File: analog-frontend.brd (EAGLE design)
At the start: 28.4 x 25.2 mm, 69 parts, among them IC1 TPS63031, IC2 ADG731, IC3 TM4C123G, IC4 INA332, IC5 NRF24L01SMD, IC6 OPA2320, Y1 CRYSTAL3X2, Y2 CRYSTAL3X2

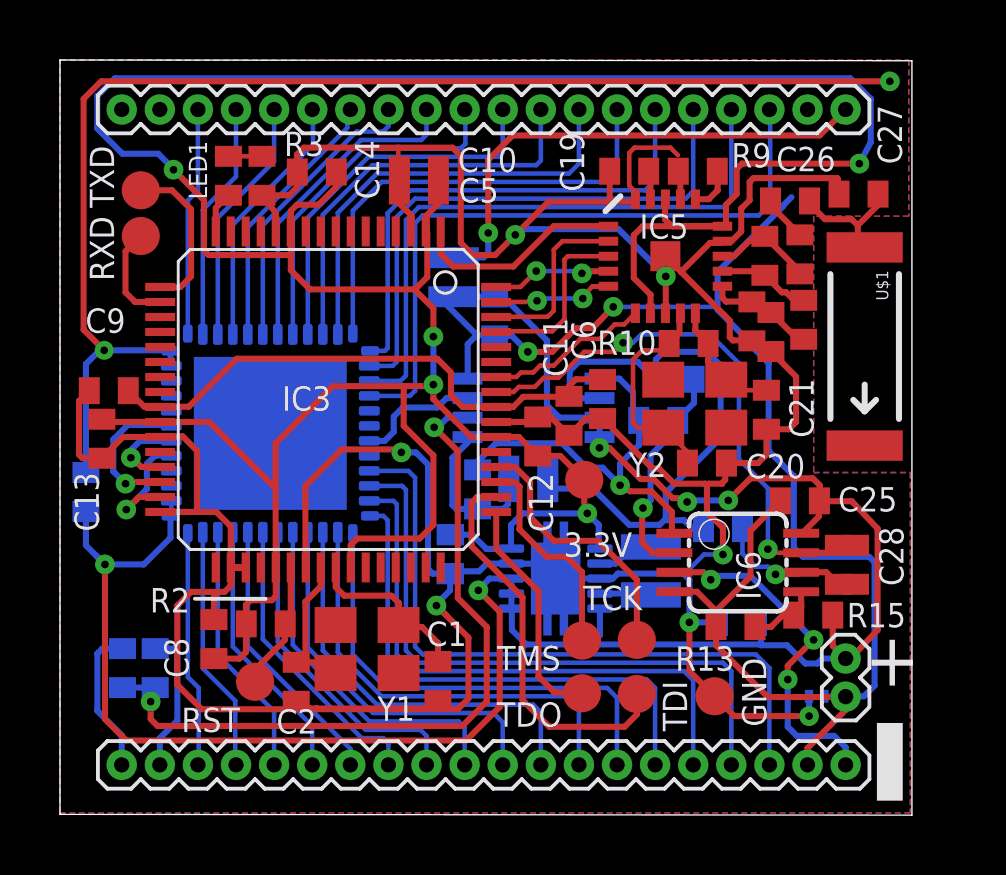
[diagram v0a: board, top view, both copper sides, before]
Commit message: added component values
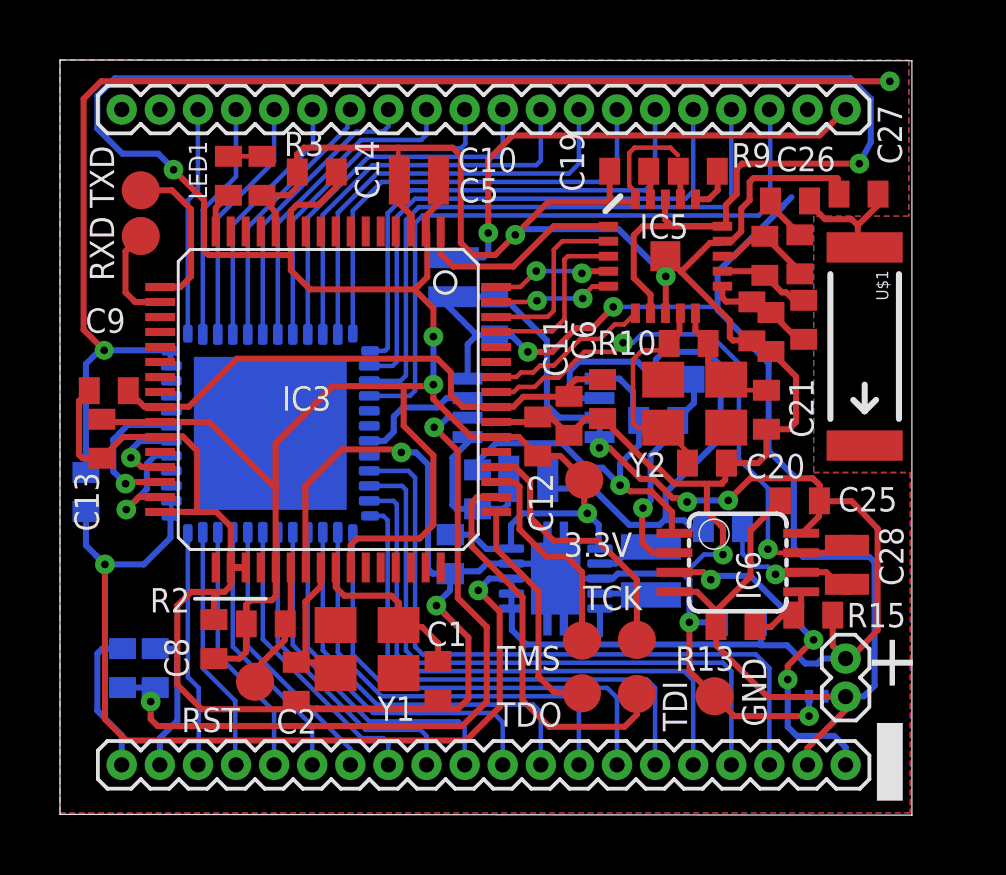
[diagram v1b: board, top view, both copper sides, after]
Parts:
- C10: value (none) -> 0.01u
- C11: value (none) -> 2.2u
- C12, C13, C15, C17, C5, C8, C9: value (none) -> 0.1u
- C14, C6: value (none) -> 1.0u
- C3: value (none) -> 4.7u
- C4, C7: value (none) -> 10u
- R2: value (none) -> 10k
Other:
- board outline removed
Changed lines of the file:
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@@
 <?xml version="1.0" encoding="utf-8"?>
 <!DOCTYPE eagle SYSTEM "eagle.dtd">
-<eagle version="6.5.0">
+<eagle version="6.6.0">
 <drawing>
 <settings>
@@
 <board>
 <plain>
-<wire x1="0" y1="0" x2="28.3972" y2="-0.0254" width="0" layer="20"/>
-<wire x1="28.3972" y1="-0.0254" x2="28.3972" y2="25.1206" width="0" layer="20"/>
-<wire x1="28.3972" y1="25.1206" x2="0" y2="25.146" width="0" layer="20"/>
-<wire x1="0" y1="25.146" x2="0" y2="0" width="0" layer="20"/>
+<wire x1="0" y1="0" x2="28.3972" y2="-0.0254" width="0" layer="21"/>
+<wire x1="28.3972" y1="-0.0254" x2="28.3972" y2="25.1206" width="0" layer="21"/>
+<wire x1="28.3972" y1="25.1206" x2="0" y2="25.146" width="0" layer="21"/>
+<wire x1="0" y1="25.146" x2="0" y2="0" width="0" layer="21"/>
 <wire x1="4.4958" y1="7.1882" x2="6.858" y2="7.1882" width="0.127" layer="25"/>
 <text x="26.8224" y="4.2926" size="1.778" layer="25">+</text>
 <text x="28.067" y="4.2926" size="1.778" layer="26" rot="MR0">+</text>
 <rectangle x1="27.2288" y1="0.4572" x2="28.0924" y2="3.048" layer="25"/>
+<wire x1="0" y1="0" x2="28.3972" y2="0" width="0" layer="22"/>
+<wire x1="28.3972" y1="0" x2="28.3972" y2="25.1206" width="0" layer="22"/>
+<wire x1="28.3972" y1="25.1206" x2="0" y2="25.1206" width="0" layer="22"/>
+<wire x1="0" y1="25.1206" x2="0" y2="0" width="0" layer="22"/>
 </plain>
 <attributes>
@@
 <attribute name="NAME" x="20.2057" y="5.8801" size="0.8128" layer="26" rot="MR0"/>
 </element>
-<element name="C3" library="rcl" package="C0402" value="" x="22.5679" y="6.4008" smashed="yes" rot="MR0">
+<element name="C3" library="rcl" package="C0402" value="4.7u" x="22.5679" y="6.4008" smashed="yes" rot="MR0">
 <attribute name="NAME" x="25.1587" y="6.6294" size="0.8128" layer="26" rot="MR0"/>
 <attribute name="VALUE" x="23.2029" y="4.4958" size="1.27" layer="28" rot="MR0"/>
 </element>
-<element name="C4" library="rcl" package="C0402" value="" x="13.0048" y="8.6741" smashed="yes" rot="MR270">
+<element name="C4" library="rcl" package="C0402" value="10u" x="13.0048" y="8.6741" smashed="yes" rot="MR270">
 <attribute name="NAME" x="12.3571" y="7.7978" size="0.8128" layer="26" rot="MR0"/>
 <attribute name="VALUE" x="14.9098" y="9.3091" size="1.27" layer="28" rot="MR270"/>
 </element>
-<element name="C7" library="rcl" package="C0402" value="" x="13.0175" y="8.6741" smashed="yes" rot="MR270">
+<element name="C7" library="rcl" package="C0402" value="10u" x="13.0175" y="8.6741" smashed="yes" rot="MR270">
 <attribute name="NAME" x="12.3063" y="8.8265" size="0.8128" layer="26" rot="MR0"/>
 <attribute name="VALUE" x="14.9225" y="9.3091" size="1.27" layer="28" rot="MR270"/>
@@
 <attribute name="VALUE" x="19.304" y="15.0368" size="1.27" layer="28" rot="MR180"/>
 </element>
-<element name="C17" library="rcl" package="C0402" value="" x="14.4907" y="16.5989" smashed="yes" rot="MR90">
+<element name="C17" library="rcl" package="C0402" value="0.1u" x="14.4907" y="16.5989" smashed="yes" rot="MR90">
 <attribute name="NAME" x="14.8209" y="16.6751" size="0.8128" layer="26" rot="MR180"/>
 <attribute name="VALUE" x="12.5857" y="15.9639" size="1.27" layer="28" rot="MR90"/>
@@
 <attribute name="VALUE" x="25.7429" y="8.5471" size="1.27" layer="27" rot="R180"/>
 </element>
-<element name="C15" library="rcl" package="C0402" value="" x="0.8636" y="10.7442" smashed="yes" rot="MR90">
+<element name="C15" library="rcl" package="C0402" value="0.1u" x="0.8636" y="10.7442" smashed="yes" rot="MR90">
 <attribute name="NAME" x="0.9144" y="11.9888" size="0.8128" layer="26" rot="MR90"/>
 <attribute name="VALUE" x="-1.0414" y="10.1092" size="1.27" layer="28" rot="MR90"/>
@@
 <attribute name="VALUE" x="5.969" y="5.0546" size="1.27" layer="27" rot="R270"/>
 </element>
-<element name="C6" library="rcl" package="C0402" value="" x="18.0848" y="13.843" smashed="yes" rot="R270">
+<element name="C6" library="rcl" package="C0402" value="1.0u" x="18.0848" y="13.843" smashed="yes" rot="R270">
 <attribute name="NAME" x="17.8562" y="15.1384" size="0.8128" layer="25" rot="R90"/>
 <attribute name="VALUE" x="16.1798" y="14.478" size="1.27" layer="27" rot="R270"/>
 </element>
-<element name="C9" library="rcl" package="C0402" value="" x="1.6256" y="14.1224" smashed="yes" rot="R180">
+<element name="C9" library="rcl" package="C0402" value="0.1u" x="1.6256" y="14.1224" smashed="yes" rot="R180">
 <attribute name="NAME" x="2.1844" y="16.8656" size="0.8128" layer="25" rot="R180"/>
 <attribute name="VALUE" x="2.2606" y="16.0274" size="1.27" layer="27" rot="R180"/>
 </element>
-<element name="C11" library="rcl" package="C0402" value="" x="16.9672" y="13.2842" smashed="yes" rot="R270">
+<element name="C11" library="rcl" package="C0402" value="2.2u" x="16.9672" y="13.2842" smashed="yes" rot="R270">
 <attribute name="NAME" x="16.9164" y="14.5796" size="0.8128" layer="25" rot="R90"/>
 <attribute name="VALUE" x="15.0622" y="13.9192" size="1.27" layer="27" rot="R270"/>
 </element>
-<element name="C5" library="rcl" package="C0402" value="" x="11.9634" y="20.7772" smashed="yes" rot="R180">
+<element name="C5" library="rcl" package="C0402" value="0.1u" x="11.9634" y="20.7772" smashed="yes" rot="R180">
 <attribute name="NAME" x="13.2842" y="20.3962" size="0.8128" layer="25"/>
 <attribute name="VALUE" x="12.5984" y="22.6822" size="1.27" layer="27" rot="R180"/>
 </element>
-<element name="C8" library="rcl" package="C0402" value="" x="5.1308" y="5.842" smashed="yes" rot="R90">
+<element name="C8" library="rcl" package="C0402" value="0.1u" x="5.1308" y="5.842" smashed="yes" rot="R90">
 <attribute name="NAME" x="4.2926" y="4.5466" size="0.8128" layer="25" rot="R90"/>
 <attribute name="VALUE" x="7.0358" y="5.207" size="1.27" layer="27" rot="R90"/>
 </element>
-<element name="C10" library="rcl" package="C0402" value="" x="11.9634" y="21.4884" smashed="yes" rot="R180">
+<element name="C10" library="rcl" package="C0402" value="0.01u" x="11.9634" y="21.4884" smashed="yes" rot="R180">
 <attribute name="NAME" x="13.2588" y="21.4122" size="0.8128" layer="25"/>
 <attribute name="VALUE" x="12.5984" y="23.3934" size="1.27" layer="27" rot="R180"/>
 </element>
-<element name="C12" library="rcl" package="C0402" value="" x="15.9258" y="12.5984" smashed="yes" rot="R90">
+<element name="C12" library="rcl" package="C0402" value="0.1u" x="15.9258" y="12.5984" smashed="yes" rot="R90">
 <attribute name="NAME" x="15.621" y="11.3792" size="0.8128" layer="25" rot="R270"/>
 <attribute name="VALUE" x="17.8308" y="11.9634" size="1.27" layer="27" rot="R90"/>
 </element>
-<element name="C13" library="rcl" package="C0402" value="" x="1.397" y="12.5222" smashed="yes" rot="R270">
+<element name="C13" library="rcl" package="C0402" value="0.1u" x="1.397" y="12.5222" smashed="yes" rot="R270">
 <attribute name="NAME" x="0.4826" y="11.4046" size="0.8128" layer="25" rot="R270"/>
 <attribute name="VALUE" x="-0.508" y="13.1572" size="1.27" layer="27" rot="R270"/>
 </element>
-<element name="C14" library="rcl" package="C0402" value="" x="8.5598" y="21.4122" smashed="yes" rot="R180">
+<element name="C14" library="rcl" package="C0402" value="1.0u" x="8.5598" y="21.4122" smashed="yes" rot="R180">
 <attribute name="NAME" x="9.8298" y="22.479" size="0.8128" layer="25" rot="R270"/>
 <attribute name="VALUE" x="9.1948" y="23.3172" size="1.27" layer="27" rot="R180"/>
 </element>
-<element name="R2" library="rcl" package="R0402" value="" x="6.858" y="6.35" smashed="yes">
+<element name="R2" library="rcl" package="R0402" value="10k" x="6.858" y="6.35" smashed="yes">
 <attribute name="NAME" x="2.9972" y="6.731" size="0.8128" layer="25"/>
 <attribute name="VALUE" x="6.223" y="4.445" size="1.27" layer="27"/>

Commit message: fixed component values
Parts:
- C1, C2, C20, C21, C28: value (none) -> 22p
- C18: value (none) -> 10p
- C19: value (none) -> 33n
- C22: value (none) -> 2.2n
- C23: value (none) -> 10n
- C24: value (none) -> 4.7p
- C25: value (none) -> 0.1u
- C26: value (none) -> 1.5p
- C27: value (none) -> 1.0p
- L2: value (none) -> 8.2n
- L3: value (none) -> 3.9n
- L4: value (none) -> 2.7n
- R10, R11, R12: value (none) -> 1M
- R13, R15, R3: value (none) -> 10k
- R5, R6, R7, R8: value (none) -> 100k
- R9: value (none) -> 22K
